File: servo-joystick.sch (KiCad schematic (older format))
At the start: 36 parts, among them P1 CONN_01X02, P2 CONN_01X03, P3 CONN_01X03, P4 CONN_01X03, P5 CONN_01X03

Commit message: Rev A
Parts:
- added TP4: CTRL1, olof:TEST_POINT_THD_NO_CIRC, symbol TEST_1P
- added TP5: INT1, olof:TEST_POINT_THD_NO_CIRC, symbol TEST_1P
- added TP6: SAW, olof:TEST_POINT_THD_NO_CIRC, symbol TEST_1P
- added TP7: BUF1, olof:TEST_POINT_THD_NO_CIRC, symbol TEST_1P
- added TP8: PWM1, olof:TEST_POINT_THD_NO_CIRC, symbol TEST_1P
- renumbered W1 to TP1, W2 to TP2, W3 to TP3
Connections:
- net Integrator #1/VIN: now also TP4.1
- net Integrator #1/VOUT: now also TP5.1
- net PWM #1/PWM: now also TP8.1
- net PWM #1/SAWTOOTH: now also TP6.1
- new net PWM #1/BUF: TP7.1
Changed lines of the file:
@@
 F3 "SAWTOOTH" I L 7950 2250 60
 F4 "VIN" I L 7950 2400 60
+F5 "BUF" O R 9100 2400 60
 $EndSheet
 $Sheet
@@
 F3 "SAWTOOTH" I L 7950 3050 60
 F4 "VIN" I L 7950 3200 60
+F5 "BUF" O R 9100 3200 60
 $EndSheet
 $Sheet
@@
 F3 "SAWTOOTH" I L 7950 3850 60
 F4 "VIN" I L 7950 4000 60
+F5 "BUF" O R 9100 4000 60
 $EndSheet
 $Sheet
@@
 F3 "SAWTOOTH" I L 7950 4650 60
 F4 "VIN" I L 7950 4800 60
+F5 "BUF" O R 9100 4800 60
 $EndSheet
 $Sheet
@@
 	7350 1450 7650 1450
 Wire Wire Line
-	7650 1450 7650 4650
+	7650 1350 7650 4650
 Wire Wire Line
 	7650 2250 7950 2250
@@
 	800  6850 800  6950
 $Comp
-L TEST_1P W1
+L TEST_1P TP1
 U 1 1 5A0CE3CF
 P 800 6850
-F 0 "W1" H 800 7120 50  0000 C CNN
+F 0 "TP1" H 800 7120 50  0000 C CNN
 F 1 "GND" H 800 7050 50  0000 C CNN
 F 2 "olof:TEST_POINT_DOUBLE_TH" H 1000 6850 50  0001 C CNN
@@
 $EndComp
 $Comp
-L TEST_1P W2
+L TEST_1P TP2
 U 1 1 5A0CE5F7
 P 1000 6850
-F 0 "W2" H 1000 7120 50  0000 C CNN
+F 0 "TP2" H 1000 7120 50  0000 C CNN
 F 1 "GND" H 1000 7050 50  0000 C CNN
 F 2 "olof:TEST_POINT_DOUBLE_TH" H 1200 6850 50  0001 C CNN
@@
 	1000 6900 1000 6850
 $Comp
-L TEST_1P W3
+L TEST_1P TP3
 U 1 1 5A0CF45B
 P 1200 6850
-F 0 "W3" H 1200 7120 50  0000 C CNN
+F 0 "TP3" H 1200 7120 50  0000 C CNN
 F 1 "GND" H 1200 7050 50  0000 C CNN
 F 2 "olof:TEST_POINT_DOUBLE_TH" H 1400 6850 50  0001 C CNN
@@
 	1200 6900 1200 6850
 Connection ~ 1000 6900
+$Comp
+L TEST_1P TP4
+U 1 1 5A2BDE71
+P 4900 2150
+F 0 "TP4" H 4900 2420 50  0000 C CNN
+F 1 "CTRL1" H 4900 2350 50  0000 C CNN
+F 2 "olof:TEST_POINT_THD_NO_CIRC" H 5100 2150 50  0001 C CNN
+F 3 "" H 5100 2150 50  0000 C CNN
+	1    4900 2150
+	1    0    0    -1
+$EndComp
+Wire Wire Line
+	4900 2150 4900 2250
+Connection ~ 4900 2250
+$Comp
+L TEST_1P TP6
+U 1 1 5A2BE649
+P 7650 1350
+F 0 "TP6" H 7650 1620 50  0000 C CNN
+F 1 "SAW" H 7650 1550 50  0000 C CNN
+F 2 "olof:TEST_POINT_THD_NO_CIRC" H 7850 1350 50  0001 C CNN
+F 3 "" H 7850 1350 50  0000 C CNN
+	1    7650 1350
+	1    0    0    -1
+$EndComp
+Connection ~ 7650 1450
+$Comp
+L TEST_1P TP5
+U 1 1 5A2BE8E0
+P 7500 2300
+F 0 "TP5" H 7500 2570 50  0000 C CNN
+F 1 "INT1" H 7500 2500 50  0000 C CNN
+F 2 "olof:TEST_POINT_THD_NO_CIRC" H 7700 2300 50  0001 C CNN
+F 3 "" H 7700 2300 50  0000 C CNN
+	1    7500 2300
+	1    0    0    -1
+$EndComp
+Wire Wire Line
+	7500 2300 7500 2400
+Connection ~ 7500 2400
+$Comp
+L TEST_1P TP8
+U 1 1 5A2BF436
+P 9500 2050
+F 0 "TP8" H 9500 2320 50  0000 C CNN
+F 1 "PWM1" H 9500 2250 50  0000 C CNN
+F 2 "olof:TEST_POINT_THD_NO_CIRC" H 9700 2050 50  0001 C CNN
+F 3 "" H 9700 2050 50  0000 C CNN
+	1    9500 2050
+	1    0    0    -1
+$EndComp
+Wire Wire Line
+	9500 2050 9500 2250
+Connection ~ 9500 2250
+$Comp
+L TEST_1P TP7
+U 1 1 5A2C1E25
+P 9250 2050
+F 0 "TP7" H 9250 2320 50  0000 C CNN
+F 1 "BUF1" H 9250 2250 50  0000 C CNN
+F 2 "olof:TEST_POINT_THD_NO_CIRC" H 9450 2050 50  0001 C CNN
+F 3 "" H 9450 2050 50  0000 C CNN
+	1    9250 2050
+	1    0    0    -1
+$EndComp
+Wire Wire Line
+	9100 2400 9250 2400
+Wire Wire Line
+	9250 2400 9250 2050
 $EndSCHEMATC

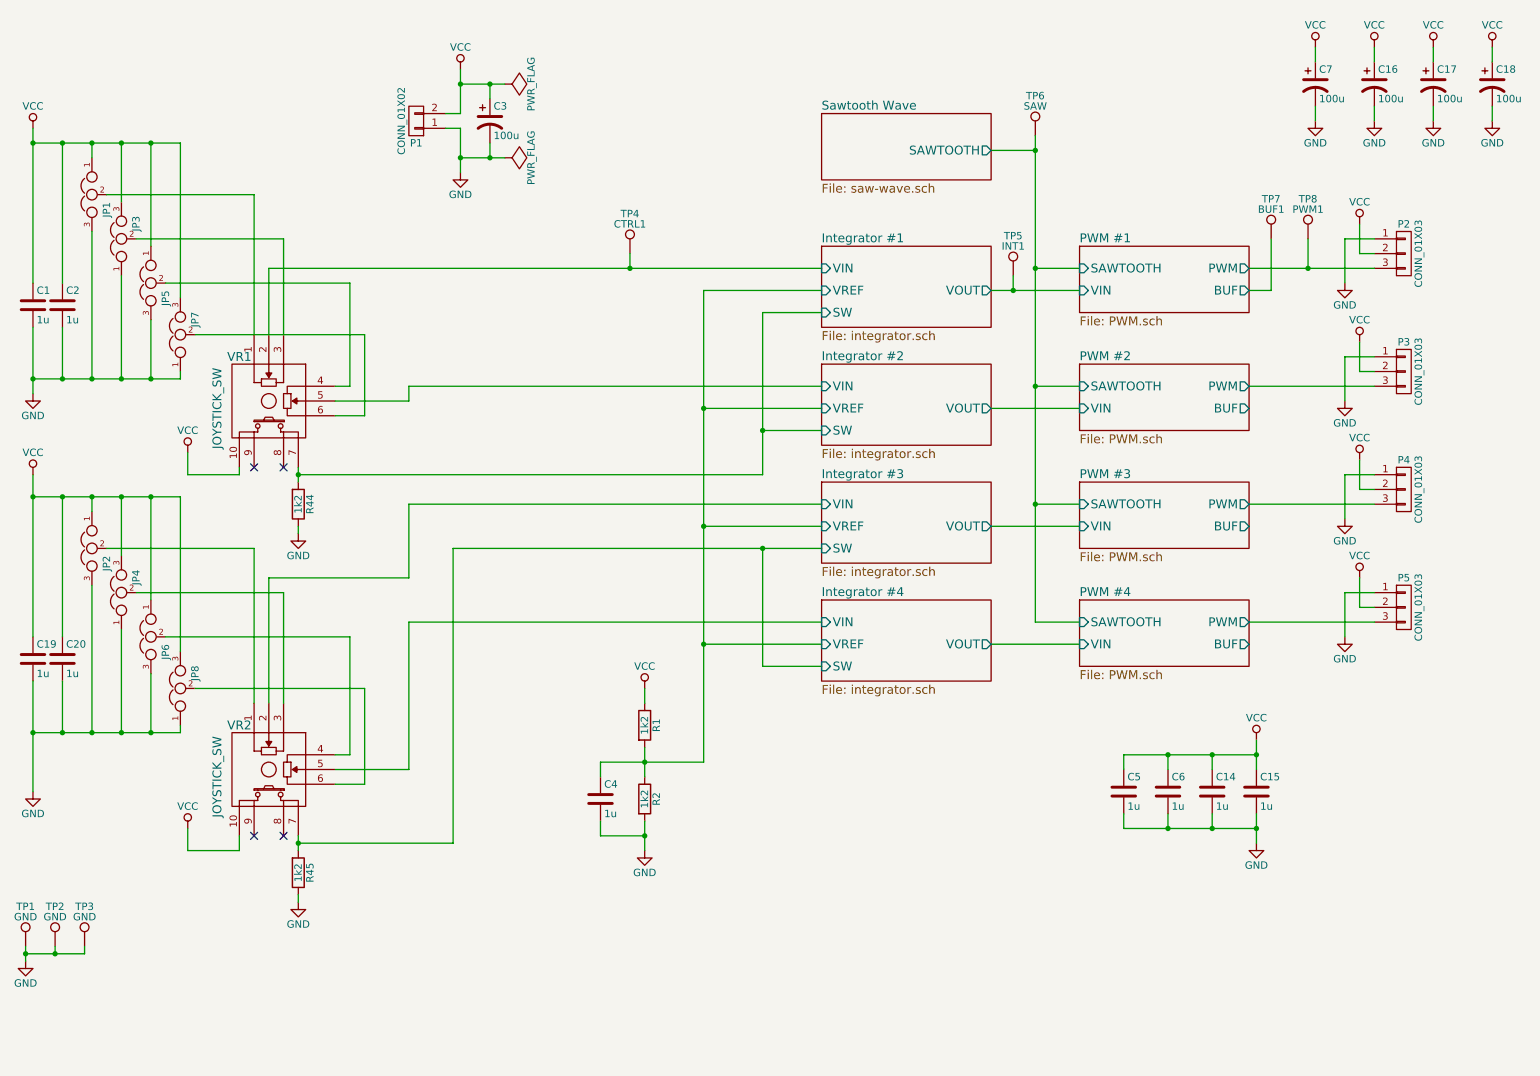
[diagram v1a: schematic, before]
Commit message: Added 5V regulator
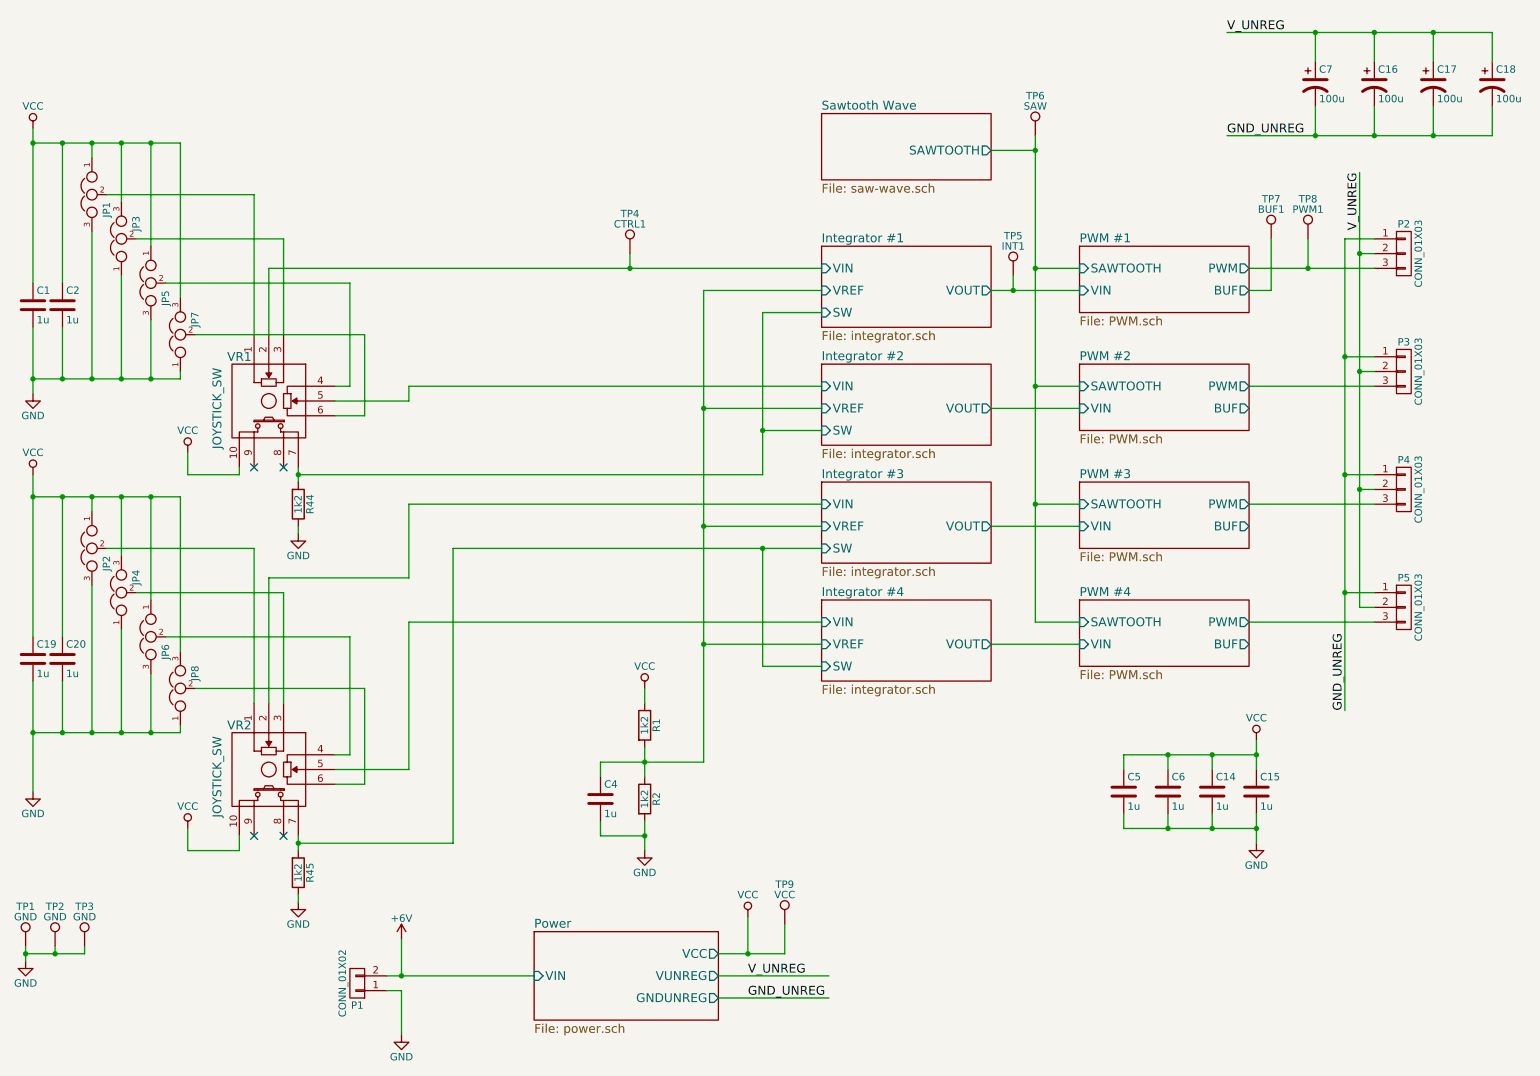
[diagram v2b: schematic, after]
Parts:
- removed C3: 100u, Capacitors_ThroughHole:C_Radial_D6.3_L11.2_P2.5, symbol CP1
- added TP9: VCC, olof:TEST_POINT_THD_NO_CIRC, symbol TEST_1P
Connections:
- net GND: no longer C16.2, C17.2, C18.2, C7.2, P2.1 (P1), P3.1 (P1), P4.1 (P1), P5.1 (P1)
- net VCC: now also TP9.1; no longer C16.1, C17.1, C18.1, C7.1, P1.2 (P2), P2.2 (P2), P3.2 (P2), P4.2 (P2), P5.2 (P2)
- new net +6V: P1.2 (P2)
- new net GND_UNREG: C16.2, C17.2, C18.2, C7.2, P2.1 (P1), P3.1 (P1), P4.1 (P1), P5.1 (P1)
- new net V_UNREG: C16.1, C17.1, C18.1, C7.1, P2.2 (P2), P3.2 (P2), P4.2 (P2), P5.2 (P2)
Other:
- moved on the sheet: P1

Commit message: Removed 0R resistors and started new layout
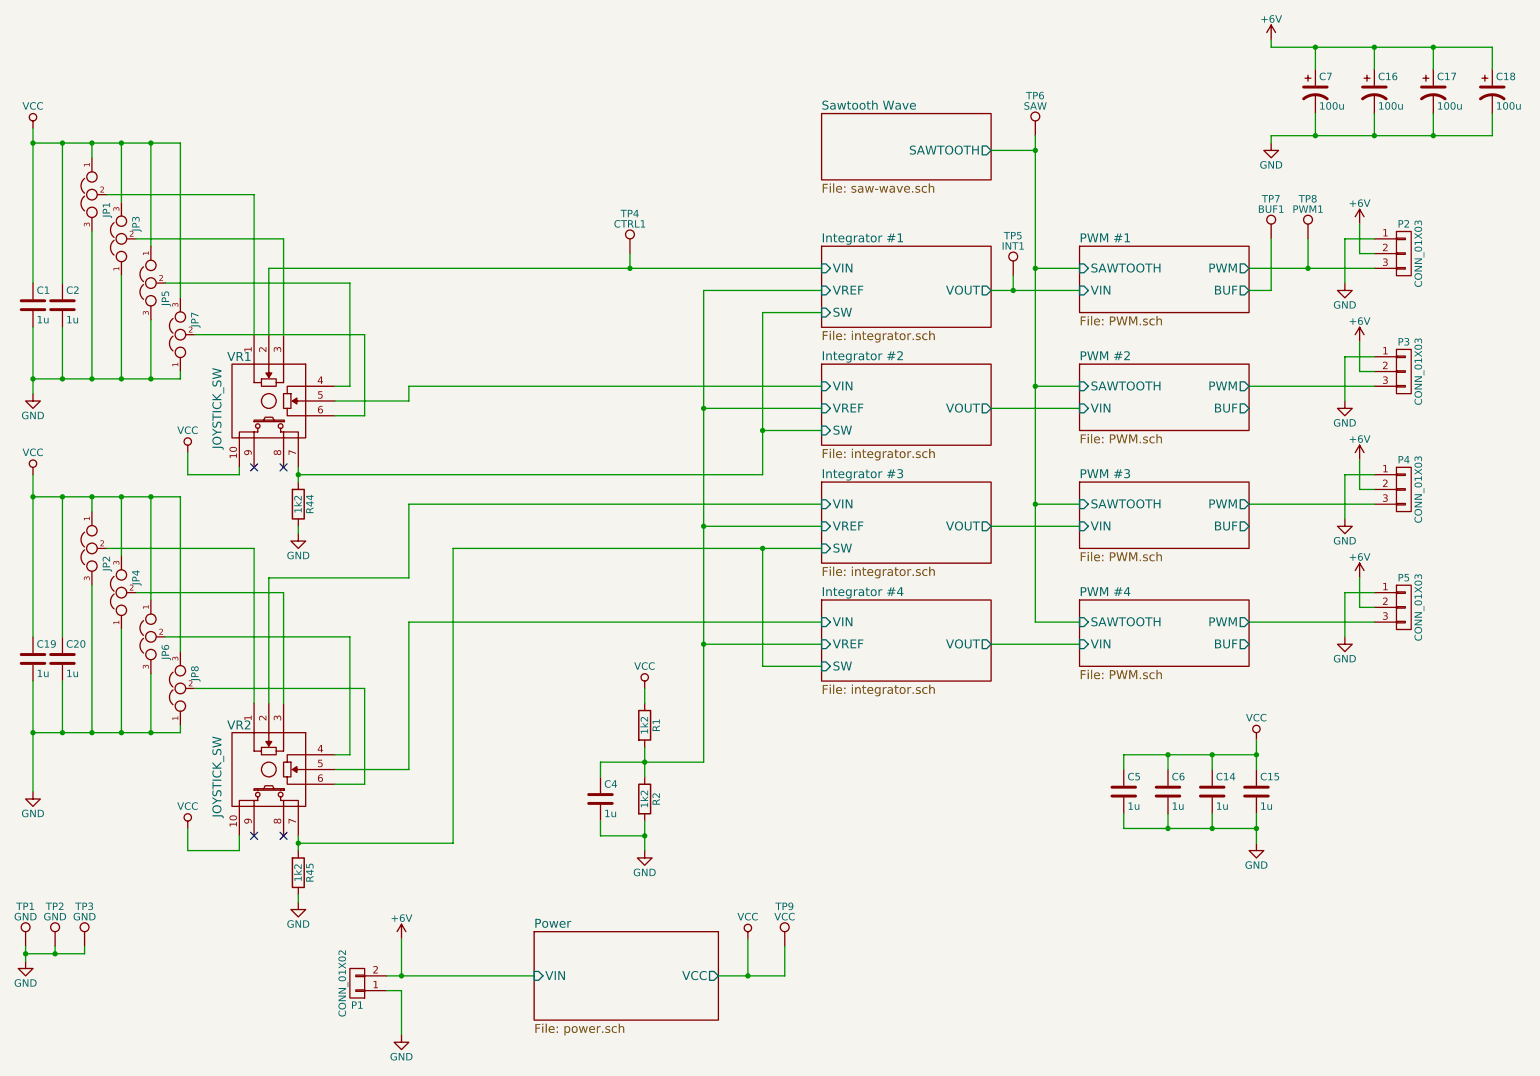
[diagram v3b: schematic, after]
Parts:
- P2, P3, P4, P5: footprint Pin_Headers:Pin_Header_Angled_1x03 -> Pin_Headers:Pin_Header_Straight_1x03
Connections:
- net GND_UNREG is gone; now on net GND: C16.2, C17.2, C18.2, C7.2, P2.1 (P1), P3.1 (P1), P4.1 (P1), P5.1 (P1)
- net V_UNREG is gone; now on net +6V: C16.1, C17.1, C18.1, C7.1, P2.2 (P2), P3.2 (P2), P4.2 (P2), P5.2 (P2)
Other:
- moved on the sheet: C16, C17, C18, C7, TP9
